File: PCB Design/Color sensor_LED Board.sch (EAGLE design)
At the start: 25 parts, among them U1 2DD2656-7

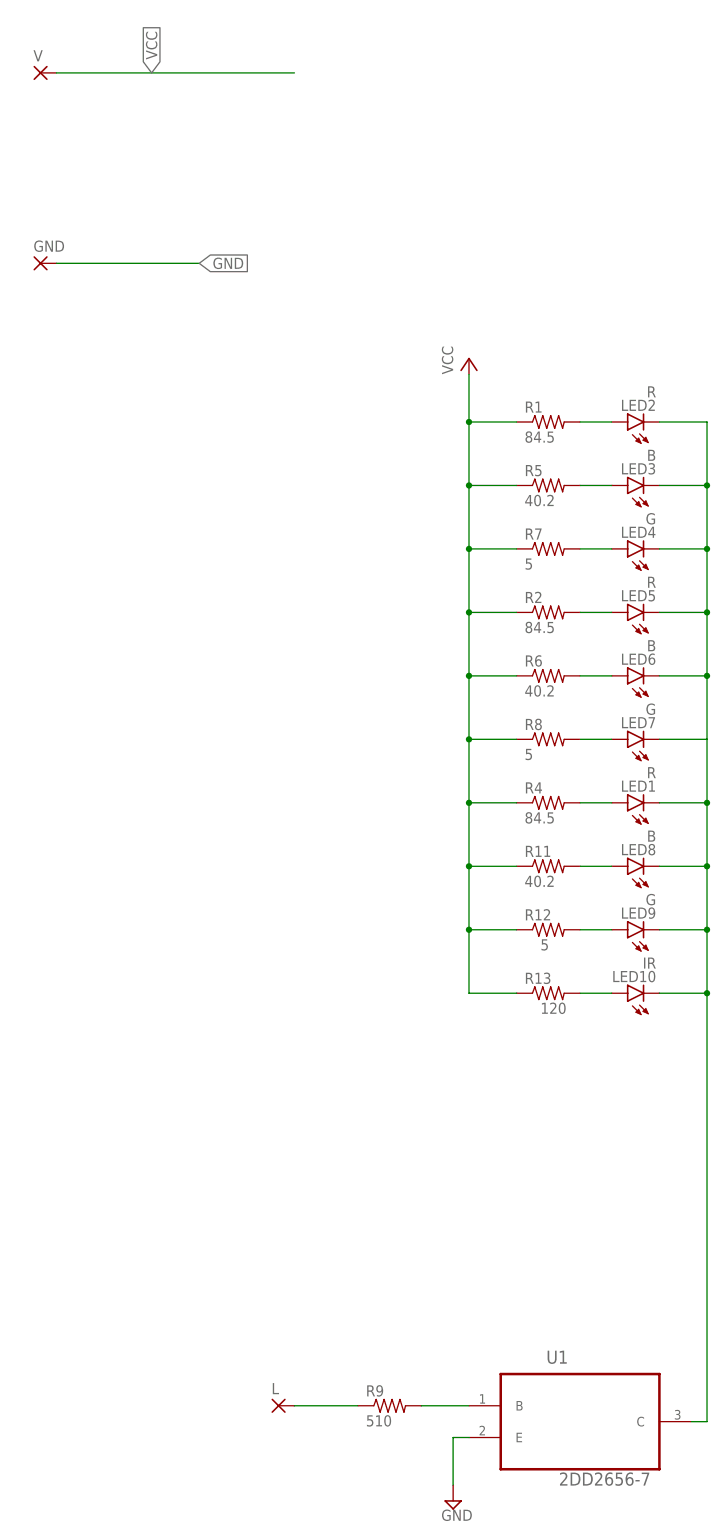
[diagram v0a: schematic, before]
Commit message: corrected unconnected traces and IR LED problem
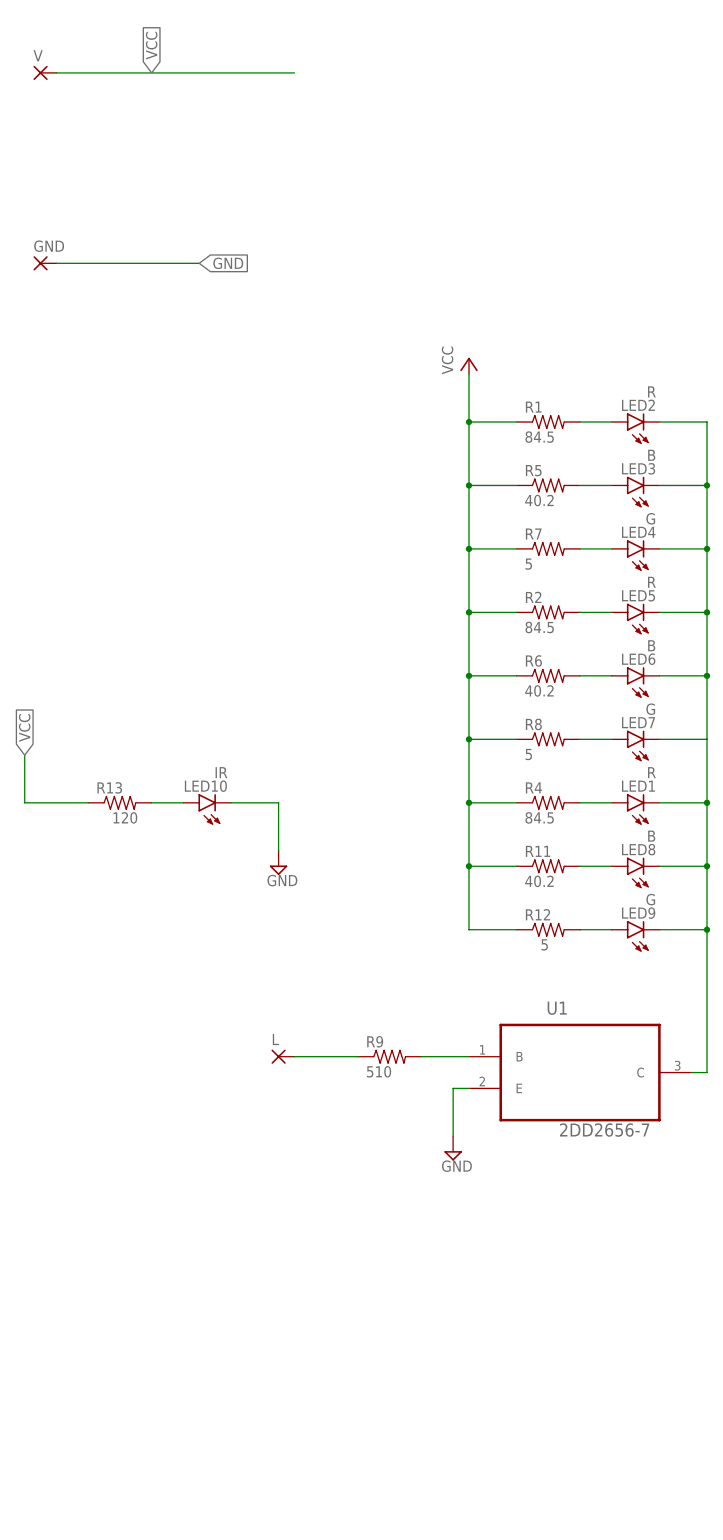
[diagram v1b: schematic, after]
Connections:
- net GND: now also LED10.C
- net N$15: no longer LED10.C
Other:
- moved on the sheet: L, LED10, R13, R9, U1
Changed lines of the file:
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@@
 <part name="LED10" library="led" library_urn="urn:adsk.eagle:library:259" deviceset="LED" device="CHIPLED_0805" package3d_urn="urn:adsk.eagle:package:15821/2" value="IR"/>
 <part name="U1" library="2DD2656-7 (1)" deviceset="2DD2656-7" device=""/>
+<part name="SUPPLY1" library="supply2" library_urn="urn:adsk.eagle:library:372" deviceset="GND" device=""/>
 </parts>
 <sheets>
@@
 <attribute name="VALUE" x="96.012" y="-47.625" size="1.778" layer="96" rot="R180"/>
 </instance>
-<instance part="SUPPLY4" gate="GND" x="63.5" y="-175.26" smashed="yes">
-<attribute name="VALUE" x="61.595" y="-178.435" size="1.778" layer="96"/>
+<instance part="SUPPLY4" gate="GND" x="63.5" y="-119.38" smashed="yes">
+<attribute name="VALUE" x="61.595" y="-122.555" size="1.778" layer="96"/>
 </instance>
 <instance part="V" gate="1" x="-2.54" y="53.34" smashed="yes">
@@
 <attribute name="VALUE" x="63.5" y="5.08" size="1.778" layer="96" rot="R90"/>
 </instance>
-<instance part="L" gate="1" x="35.56" y="-160.02" smashed="yes">
-<attribute name="NAME" x="34.417" y="-158.1658" size="1.778" layer="95"/>
-<attribute name="VALUE" x="34.417" y="-163.322" size="1.778" layer="96"/>
+<instance part="L" gate="1" x="35.56" y="-104.14" smashed="yes">
+<attribute name="NAME" x="34.417" y="-102.2858" size="1.778" layer="95"/>
+<attribute name="VALUE" x="34.417" y="-107.442" size="1.778" layer="96"/>
 </instance>
 <instance part="R1" gate="G$1" x="78.74" y="-2.54" smashed="yes">
@@
 <attribute name="VALUE" x="74.93" y="-56.642" size="1.778" layer="96"/>
 </instance>
-<instance part="R9" gate="G$1" x="53.34" y="-160.02" smashed="yes">
-<attribute name="NAME" x="49.53" y="-158.5214" size="1.778" layer="95"/>
-<attribute name="VALUE" x="49.53" y="-163.322" size="1.778" layer="96"/>
+<instance part="R9" gate="G$1" x="53.34" y="-104.14" smashed="yes">
+<attribute name="NAME" x="49.53" y="-102.6414" size="1.778" layer="95"/>
+<attribute name="VALUE" x="49.53" y="-107.442" size="1.778" layer="96"/>
 </instance>
 <instance part="LED1" gate="G$1" x="91.44" y="-63.5" smashed="yes" rot="R90">
@@
 <attribute name="VALUE" x="77.47" y="-87.122" size="1.778" layer="96"/>
 </instance>
-<instance part="R13" gate="G$1" x="78.74" y="-93.98" smashed="yes">
-<attribute name="NAME" x="74.93" y="-92.4814" size="1.778" layer="95"/>
-<attribute name="VALUE" x="77.47" y="-97.282" size="1.778" layer="96"/>
-</instance>
-<instance part="LED10" gate="G$1" x="91.44" y="-93.98" smashed="yes" rot="R90">
-<attribute name="NAME" x="96.012" y="-90.424" size="1.778" layer="95" rot="R180"/>
-<attribute name="VALUE" x="96.012" y="-88.265" size="1.778" layer="96" rot="R180"/>
-</instance>
-<instance part="U1" gate="A" x="83.82" y="-160.02" smashed="yes">
-<attribute name="NAME" x="78.4066" y="-153.28501875" size="2.08403125" layer="95" ratio="10" rot="SR0"/>
-<attribute name="VALUE" x="80.41568125" y="-172.7989" size="2.083240625" layer="96" ratio="10" rot="SR0"/>
+<instance part="R13" gate="G$1" x="10.16" y="-63.5" smashed="yes">
+<attribute name="NAME" x="6.35" y="-62.0014" size="1.778" layer="95"/>
+<attribute name="VALUE" x="8.89" y="-66.802" size="1.778" layer="96"/>
+</instance>
+<instance part="LED10" gate="G$1" x="22.86" y="-63.5" smashed="yes" rot="R90">
+<attribute name="NAME" x="27.432" y="-59.944" size="1.778" layer="95" rot="R180"/>
+<attribute name="VALUE" x="27.432" y="-57.785" size="1.778" layer="96" rot="R180"/>
+</instance>
+<instance part="U1" gate="A" x="83.82" y="-104.14" smashed="yes">
+<attribute name="NAME" x="78.4066" y="-97.40501875" size="2.08403125" layer="95" ratio="10" rot="SR0"/>
+<attribute name="VALUE" x="80.41568125" y="-116.9189" size="2.083240625" layer="96" ratio="10" rot="SR0"/>
+</instance>
+<instance part="SUPPLY1" gate="GND" x="35.56" y="-73.66" smashed="yes">
+<attribute name="VALUE" x="33.655" y="-76.835" size="1.778" layer="96"/>
 </instance>
 </instances>
@@
 <segment>
 <pinref part="SUPPLY4" gate="GND" pin="GND"/>
-<wire x1="63.5" y1="-172.72" x2="63.5" y2="-165.1" width="0.1524" layer="91"/>
+<wire x1="63.5" y1="-116.84" x2="63.5" y2="-109.22" width="0.1524" layer="91"/>
 <pinref part="U1" gate="A" pin="E"/>
-<wire x1="63.5" y1="-165.1" x2="66.04" y2="-165.1" width="0.1524" layer="91"/>
+<wire x1="63.5" y1="-109.22" x2="66.04" y2="-109.22" width="0.1524" layer="91"/>
 </segment>
 <segment>
@@
 <wire x1="22.86" y1="22.86" x2="0" y2="22.86" width="0.1524" layer="91"/>
 <label x="22.86" y="22.86" size="1.778" layer="95" xref="yes"/>
+</segment>
+<segment>
+<pinref part="LED10" gate="G$1" pin="C"/>
+<wire x1="27.94" y1="-63.5" x2="35.56" y2="-63.5" width="0.1524" layer="91"/>
+<wire x1="35.56" y1="-63.5" x2="35.56" y2="-71.12" width="0.1524" layer="91"/>
+<pinref part="SUPPLY1" gate="GND" pin="GND"/>
 </segment>
 </net>
@@
 <pinref part="R11" gate="G$1" pin="1"/>
 <pinref part="R12" gate="G$1" pin="1"/>
-<pinref part="R13" gate="G$1" pin="1"/>
-<wire x1="73.66" y1="-93.98" x2="66.04" y2="-93.98" width="0.1524" layer="91"/>
-<wire x1="66.04" y1="-93.98" x2="66.04" y2="-83.82" width="0.1524" layer="91"/>
-<junction x="66.04" y="-83.82"/>
 <pinref part="R8" gate="G$1" pin="1"/>
 <wire x1="73.66" y1="-53.34" x2="66.04" y2="-53.34" width="0.1524" layer="91"/>
 <junction x="66.04" y="-53.34"/>
 </segment>
+<segment>
+<pinref part="R13" gate="G$1" pin="1"/>
+<wire x1="5.08" y1="-63.5" x2="-5.08" y2="-63.5" width="0.1524" layer="91"/>
+<wire x1="-5.08" y1="-63.5" x2="-5.08" y2="-55.88" width="0.1524" layer="91"/>
+<label x="-5.08" y="-55.88" size="1.778" layer="95" rot="R90" xref="yes"/>
+</segment>
 </net>
 <net name="N$6" class="0">
@@
 <net name="N$2" class="0">
 <segment>
-<wire x1="66.04" y1="-160.02" x2="58.42" y2="-160.02" width="0.1524" layer="91"/>
+<wire x1="66.04" y1="-104.14" x2="58.42" y2="-104.14" width="0.1524" layer="91"/>
 <pinref part="R9" gate="G$1" pin="2"/>
 <pinref part="U1" gate="A" pin="B"/>
@@
 <net name="N$4" class="0">
 <segment>
-<wire x1="48.26" y1="-160.02" x2="38.1" y2="-160.02" width="0.1524" layer="91"/>
+<wire x1="48.26" y1="-104.14" x2="38.1" y2="-104.14" width="0.1524" layer="91"/>
 <pinref part="L" gate="1" pin="P"/>
 <pinref part="R9" gate="G$1" pin="1"/>
@@
 <pinref part="R13" gate="G$1" pin="2"/>
 <pinref part="LED10" gate="G$1" pin="A"/>
-<wire x1="83.82" y1="-93.98" x2="88.9" y2="-93.98" width="0.1524" layer="91"/>
+<wire x1="15.24" y1="-63.5" x2="20.32" y2="-63.5" width="0.1524" layer="91"/>
 </segment>
 </net>
@@
 <segment>
 <pinref part="U1" gate="A" pin="C"/>
-<wire x1="101.6" y1="-162.56" x2="104.14" y2="-162.56" width="0.1524" layer="91"/>
+<wire x1="101.6" y1="-106.68" x2="104.14" y2="-106.68" width="0.1524" layer="91"/>
 <wire x1="104.14" y1="-2.54" x2="104.14" y2="-12.7" width="0.1524" layer="91"/>
 <pinref part="LED2" gate="G$1" pin="C"/>
@@
 <pinref part="LED9" gate="G$1" pin="C"/>
 <wire x1="96.52" y1="-83.82" x2="104.14" y2="-83.82" width="0.1524" layer="91"/>
-<pinref part="LED10" gate="G$1" pin="C"/>
-<wire x1="96.52" y1="-93.98" x2="104.14" y2="-93.98" width="0.1524" layer="91"/>
-<wire x1="104.14" y1="-93.98" x2="104.14" y2="-83.82" width="0.1524" layer="91"/>
 <junction x="104.14" y="-83.82"/>
-<wire x1="104.14" y1="-162.56" x2="104.14" y2="-93.98" width="0.1524" layer="91"/>
-<junction x="104.14" y="-93.98"/>
-</segment>
-</net>
+<wire x1="104.14" y1="-106.68" x2="104.14" y2="-83.82" width="0.1524" layer="91"/>
+</segment>
+</net>
